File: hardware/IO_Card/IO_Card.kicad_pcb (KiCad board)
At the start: 2 copper layers, 79.5 x 99.9 mm, 18 parts, among them J1 6502 Edge, J2 6502 Pinheader, J3 Port A, J4 Port B, J7 Port A, J8 Port B, J9 VIA IO Select, U1 W65C22NxP, U2 W65C22NxP

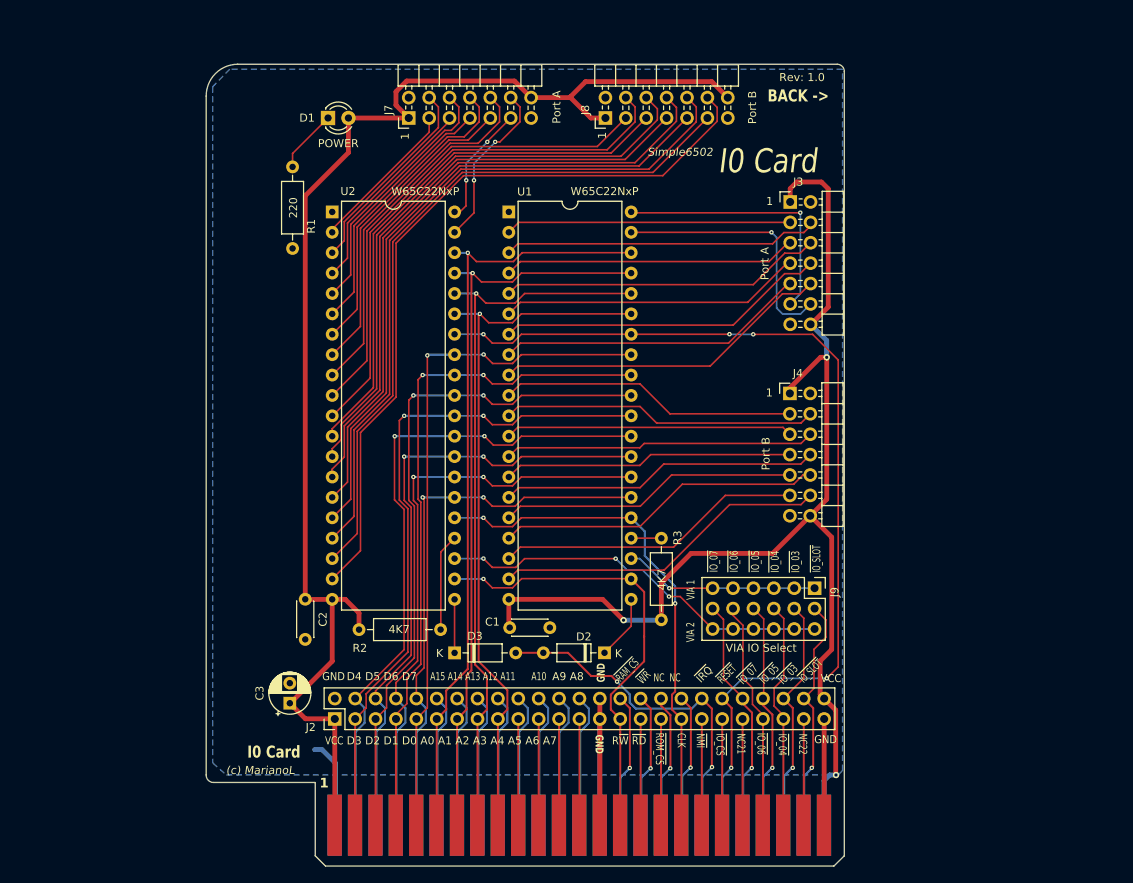
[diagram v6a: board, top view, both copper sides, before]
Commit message: IOCard with SMD bypass caps
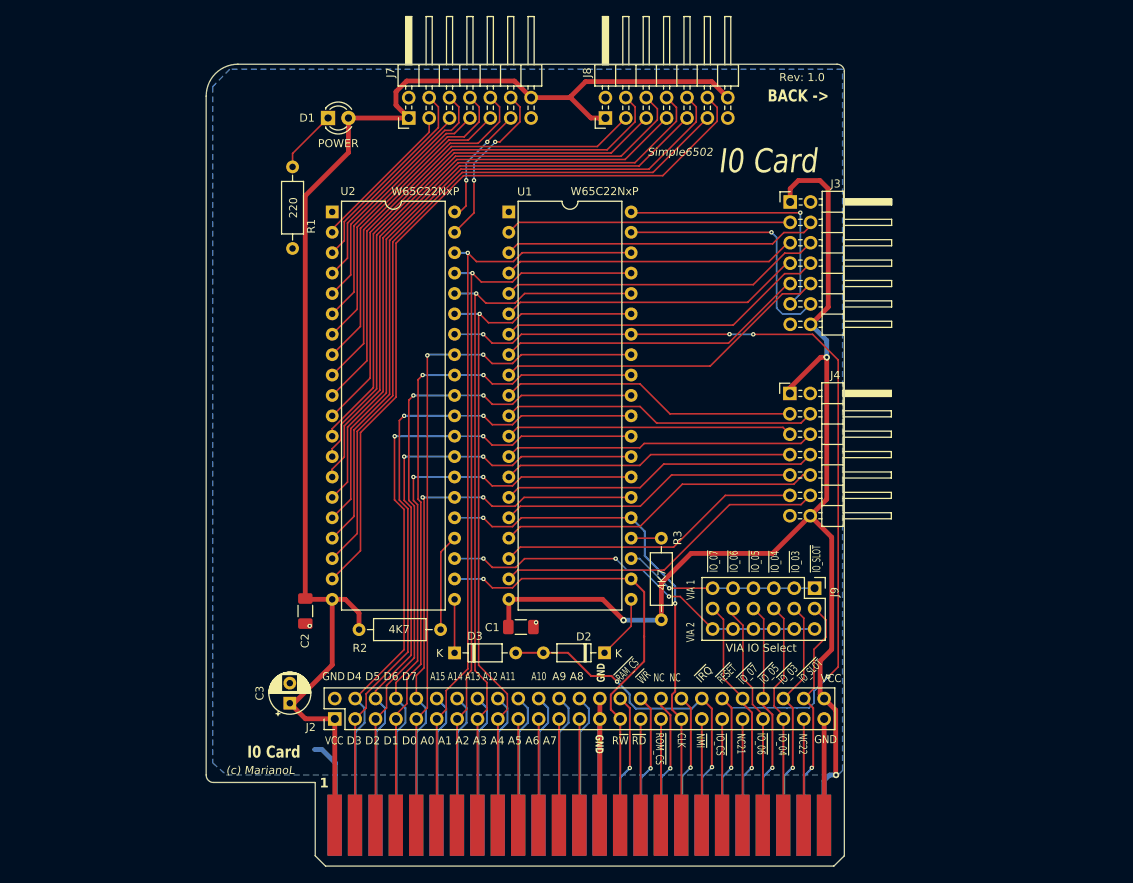
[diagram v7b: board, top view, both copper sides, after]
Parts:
- C1, C2: footprint Capacitor_THT:C_Disc_D4.3mm_W1.9mm_P5.00mm -> Capacitor_SMD:C_1206_3216Metric_Pad1.33x1.80mm_HandSolder
- J3, J4, J7, J8: footprint Connector_PinHeader_2.54mm:PinHeader_2x07_P2.54mm_Horizontal_Edge -> Connector_PinHeader_2.54mm:PinHeader_2x07_P2.54mm_Horizontal
- moved C2 1.47 mm to (52.6, 98.7)
- moved C1 1.39 mm to (79.5, 100.7)
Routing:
- net /~{RESET}: track 121.1 -> 123.0 mm
- net GND: vias 0 -> 2

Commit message: IO Card rev 1.1 + smd caps
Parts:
- moved R3 0.23 mm to (96.8, 89.6)
